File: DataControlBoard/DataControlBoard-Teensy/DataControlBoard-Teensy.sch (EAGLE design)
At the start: 23 parts, among them IC1 74LS165D, IC2 74LS165D, J1 RS-Interface, J2 Pwr-Conn, J3 Static RPi, J4 Magnet RPi, J5 Laser RPi, U1 MAX3232, U2 3V3REG

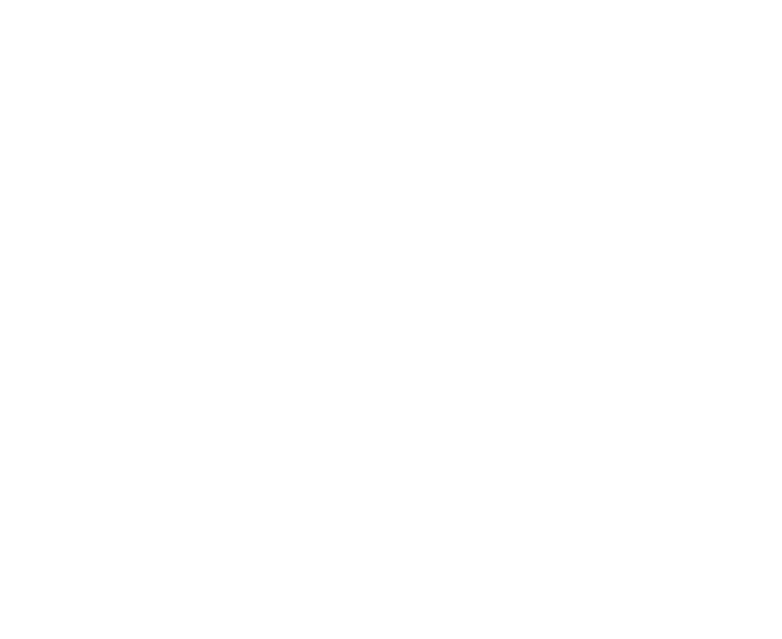
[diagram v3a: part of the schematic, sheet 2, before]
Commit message: Rearranged DataControl-Teensy
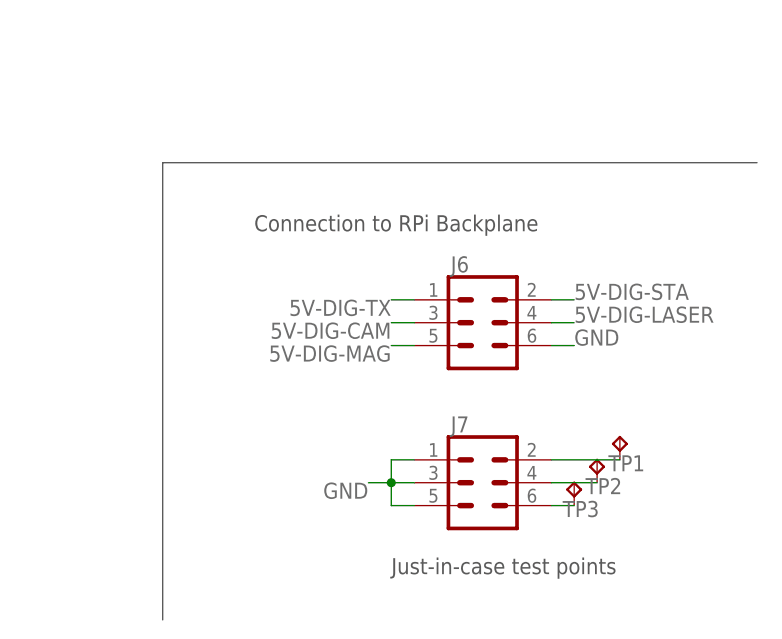
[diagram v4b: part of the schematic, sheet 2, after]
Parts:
- added J6, J7: (no value), SparkFun-Connectors:CONN_03X22X3_SILK_MALE_PTH
- added TP1, TP2, TP3: TPPAD1-17, testpad:TPPAD1-17
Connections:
- new net N$27: J7.4, TP2.TP
- new net N$28: J7.6, TP3.TP
- new net N$6: J7.2, TP1.TP
- net 5V-DIG-CAM: now also J6.3
- net 5V-DIG-LASER: now also J6.4
- net 5V-DIG-MAG: now also J6.5
- net 5V-DIG-STA: now also J6.2
- net 5V-DIG-TX: now also J6.1
- net GND: now also J6.6, J7.1, J7.3, J7.5
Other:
- note added: "Connection to RPi Backplane"
- note added: "Just-in-case test points"
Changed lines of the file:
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@@
 <part name="R8" library="rcl" library_urn="urn:adsk.eagle:library:334" deviceset="R-US_" device="R0805" package3d_urn="urn:adsk.eagle:package:23553/2" value="15k"/>
 <part name="GND5" library="supply1" library_urn="urn:adsk.eagle:library:371" deviceset="GND" device=""/>
+<part name="J6" library="SparkFun-Connectors" library_urn="urn:adsk.eagle:library:513" deviceset="CONN_03X2" device="2X3_SILK_MALE_PTH" package3d_urn="urn:adsk.eagle:package:38016/1"/>
+<part name="J7" library="SparkFun-Connectors" library_urn="urn:adsk.eagle:library:513" deviceset="CONN_03X2" device="2X3_SILK_MALE_PTH" package3d_urn="urn:adsk.eagle:package:38016/1"/>
+<part name="TP1" library="testpad" library_urn="urn:adsk.eagle:library:385" deviceset="TP" device="PAD1-17" package3d_urn="urn:adsk.eagle:package:27949/1"/>
+<part name="TP2" library="testpad" library_urn="urn:adsk.eagle:library:385" deviceset="TP" device="PAD1-17" package3d_urn="urn:adsk.eagle:package:27949/1"/>
+<part name="TP3" library="testpad" library_urn="urn:adsk.eagle:library:385" deviceset="TP" device="PAD1-17" package3d_urn="urn:adsk.eagle:package:27949/1"/>
 </parts>
 <sheets>
@@
 <wire x1="236.22" y1="121.92" x2="236.22" y2="104.14" width="0.1524" layer="97"/>
 <text x="226.06" y="127" size="1.778" layer="97" align="top-left">GPIO from Pi:</text>
+<text x="215.9" y="30.48" size="1.778" layer="97">Just-in-case test points</text>
+<text x="200.66" y="68.58" size="1.778" layer="97">Connection to RPi Backplane</text>
+<wire x1="190.5" y1="25.4" x2="190.5" y2="76.2" width="0.1524" layer="97"/>
+<wire x1="190.5" y1="76.2" x2="256.54" y2="76.2" width="0.1524" layer="97"/>
 </plain>
 <instances>
@@
 <attribute name="NAME" x="35.56" y="98.679" size="1.778" layer="95" font="vector" rot="R180"/>
 <attribute name="VALUE" x="35.56" y="99.441" size="1.778" layer="96" font="vector" rot="R180" align="top-left"/>
+</instance>
+<instance part="J6" gate="G$1" x="226.06" y="58.42" smashed="yes">
+<attribute name="NAME" x="222.504" y="64.008" size="1.778" layer="95" font="vector"/>
+<attribute name="VALUE" x="222.758" y="52.578" size="1.778" layer="96" font="vector" align="top-left"/>
+</instance>
+<instance part="J7" gate="G$1" x="226.06" y="40.64" smashed="yes">
+<attribute name="NAME" x="222.504" y="46.228" size="1.778" layer="95" font="vector"/>
+<attribute name="VALUE" x="222.758" y="34.798" size="1.778" layer="96" font="vector" align="top-left"/>
+</instance>
+<instance part="TP1" gate="G$1" x="241.3" y="45.72" smashed="yes">
+<attribute name="NAME" x="240.03" y="41.91" size="1.778" layer="95"/>
+<attribute name="TP_SIGNAL_NAME" x="242.57" y="44.45" size="1.778" layer="97"/>
+</instance>
+<instance part="TP2" gate="G$1" x="238.76" y="43.18" smashed="yes">
+<attribute name="NAME" x="237.49" y="39.37" size="1.778" layer="95"/>
+<attribute name="TP_SIGNAL_NAME" x="240.03" y="41.91" size="1.778" layer="97"/>
+</instance>
+<instance part="TP3" gate="G$1" x="236.22" y="40.64" smashed="yes">
+<attribute name="NAME" x="234.95" y="36.83" size="1.778" layer="95"/>
+<attribute name="TP_SIGNAL_NAME" x="237.49" y="39.37" size="1.778" layer="97"/>
 </instance>
 </instances>
@@
 </segment>
 </net>
+<net name="GND" class="0">
+<segment>
+<pinref part="J7" gate="G$1" pin="1"/>
+<wire x1="218.44" y1="43.18" x2="215.9" y2="43.18" width="0.1524" layer="91"/>
+<wire x1="215.9" y1="43.18" x2="215.9" y2="40.64" width="0.1524" layer="91"/>
+<pinref part="J7" gate="G$1" pin="5"/>
+<wire x1="215.9" y1="40.64" x2="215.9" y2="38.1" width="0.1524" layer="91"/>
+<wire x1="215.9" y1="38.1" x2="218.44" y2="38.1" width="0.1524" layer="91"/>
+<pinref part="J7" gate="G$1" pin="3"/>
+<wire x1="218.44" y1="40.64" x2="215.9" y2="40.64" width="0.1524" layer="91"/>
+<junction x="215.9" y="40.64"/>
+<wire x1="215.9" y1="40.64" x2="213.36" y2="40.64" width="0.1524" layer="91"/>
+<label x="213.36" y="40.64" size="1.778" layer="95" rot="R180"/>
+</segment>
+<segment>
+<pinref part="J6" gate="G$1" pin="6"/>
+<wire x1="233.68" y1="55.88" x2="236.22" y2="55.88" width="0.1524" layer="91"/>
+<label x="236.22" y="55.88" size="1.778" layer="95"/>
+</segment>
+</net>
+<net name="5V-DIG-LASER" class="0">
+<segment>
+<pinref part="J6" gate="G$1" pin="4"/>
+<wire x1="233.68" y1="58.42" x2="236.22" y2="58.42" width="0.1524" layer="91"/>
+<label x="236.22" y="58.42" size="1.778" layer="95"/>
+</segment>
+</net>
+<net name="5V-DIG-STA" class="0">
+<segment>
+<pinref part="J6" gate="G$1" pin="2"/>
+<wire x1="233.68" y1="60.96" x2="236.22" y2="60.96" width="0.1524" layer="91"/>
+<label x="236.22" y="60.96" size="1.778" layer="95"/>
+</segment>
+</net>
+<net name="5V-DIG-TX" class="0">
+<segment>
+<pinref part="J6" gate="G$1" pin="1"/>
+<wire x1="218.44" y1="60.96" x2="215.9" y2="60.96" width="0.1524" layer="91"/>
+<label x="215.9" y="60.96" size="1.778" layer="95" rot="R180"/>
+</segment>
+</net>
+<net name="5V-DIG-CAM" class="0">
+<segment>
+<pinref part="J6" gate="G$1" pin="3"/>
+<wire x1="218.44" y1="58.42" x2="215.9" y2="58.42" width="0.1524" layer="91"/>
+<label x="215.9" y="58.42" size="1.778" layer="95" rot="R180"/>
+</segment>
+</net>
+<net name="5V-DIG-MAG" class="0">
+<segment>
+<pinref part="J6" gate="G$1" pin="5"/>
+<wire x1="218.44" y1="55.88" x2="215.9" y2="55.88" width="0.1524" layer="91"/>
+<label x="215.9" y="55.88" size="1.778" layer="95" rot="R180"/>
+</segment>
+</net>
+<net name="N$6" class="0">
+<segment>
+<pinref part="J7" gate="G$1" pin="2"/>
+<pinref part="TP1" gate="G$1" pin="TP"/>
+<wire x1="233.68" y1="43.18" x2="241.3" y2="43.18" width="0.1524" layer="91"/>
+</segment>
+</net>
+<net name="N$27" class="0">
+<segment>
+<pinref part="TP2" gate="G$1" pin="TP"/>
+<pinref part="J7" gate="G$1" pin="4"/>
+<wire x1="238.76" y1="40.64" x2="233.68" y2="40.64" width="0.1524" layer="91"/>
+</segment>
+</net>
+<net name="N$28" class="0">
+<segment>
+<pinref part="J7" gate="G$1" pin="6"/>
+<pinref part="TP3" gate="G$1" pin="TP"/>
+<wire x1="233.68" y1="38.1" x2="236.22" y2="38.1" width="0.1524" layer="91"/>
+</segment>
+</net>

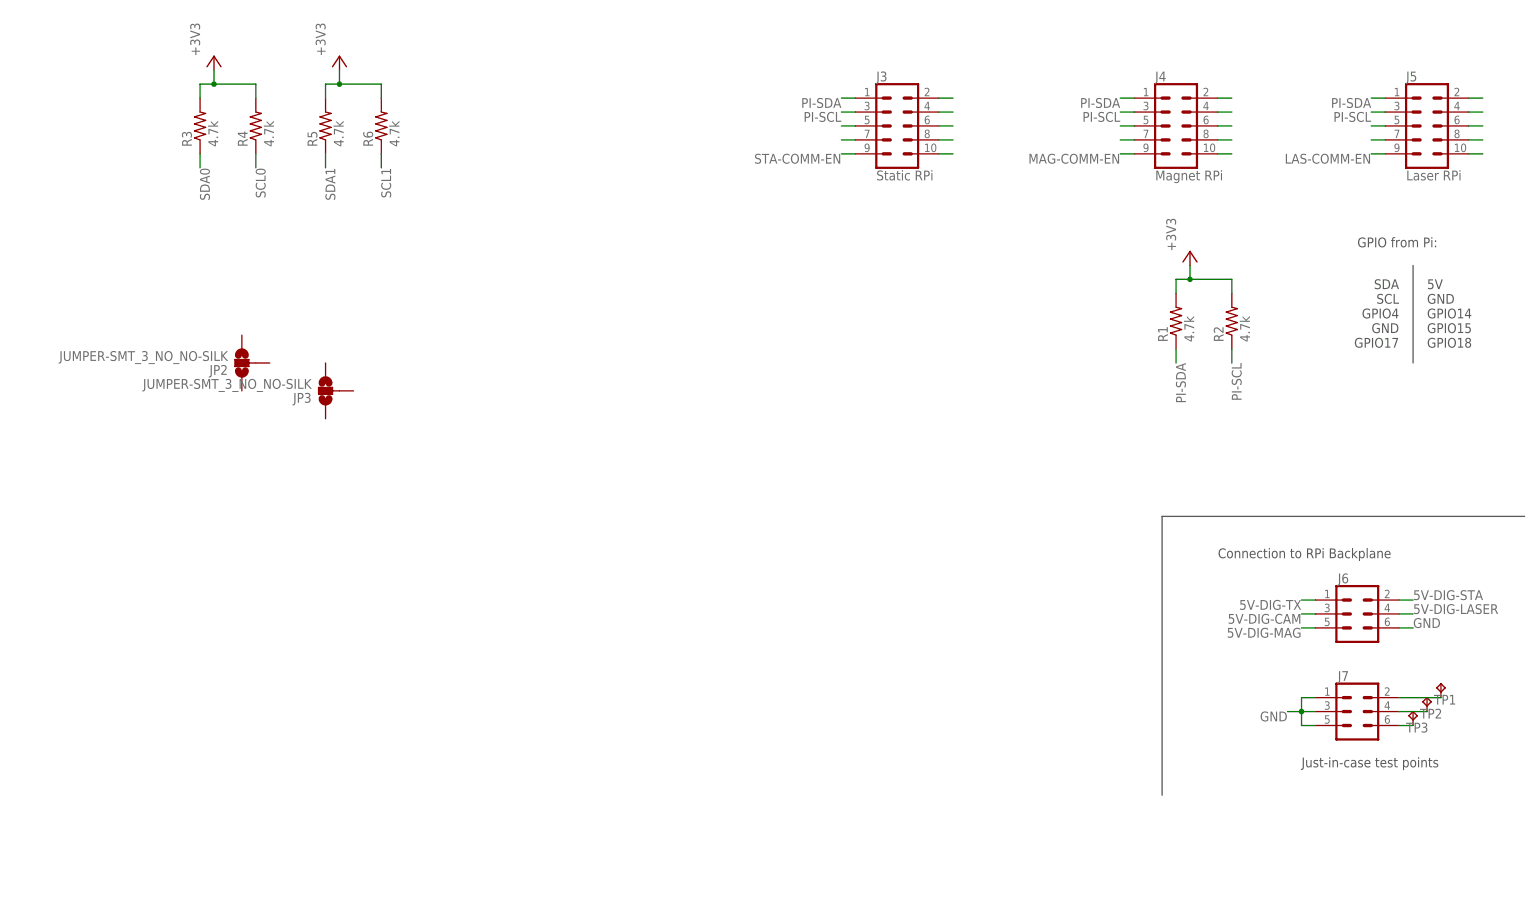
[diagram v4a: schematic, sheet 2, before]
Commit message: Added jumper selection for sda/scl and wired rs232 converter
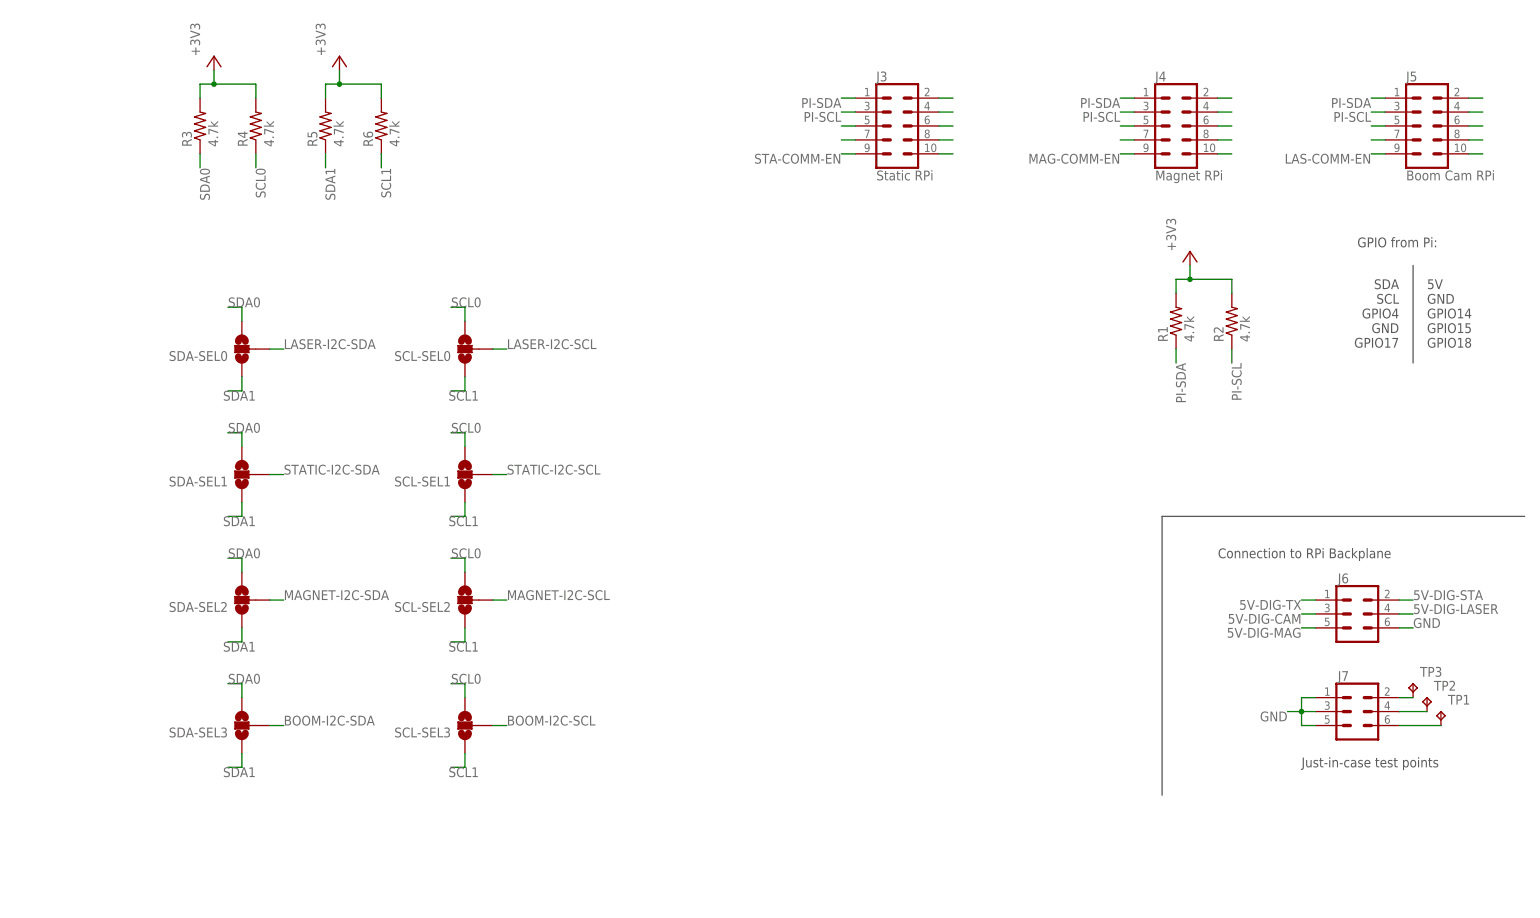
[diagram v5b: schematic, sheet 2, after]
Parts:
- removed JP2, JP3: JUMPER-SMT_3_NO_NO-SILK, SparkFun-Jumpers:JUMPER-SMT_3_NO_NO-SILK
- added C3, C4, C5, C6: 0.1uF, rcl:C-USC0805
- added SCL-SEL0, SCL-SEL1, SCL-SEL2, SCL-SEL3, SDA-SEL0, SDA-SEL1, SDA-SEL2, SDA-SEL3: JUMPER-SMT_3_NO_NO-SILK, SparkFun-Jumpers:JUMPER-SMT_3_NO_NO-SILK
- J5: value Laser RPi -> Boom Cam RPi
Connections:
- removed net N$1: IC1A.CLK, IC2A.CLK
- removed net N$12: B1.3*
- removed net N$20: B1.4*
- removed net N$26: B1.5*
- new net N$32: C5.1, U1.V+
- new net N$33: C6.1, U1.V-
- new net N$34: C3.1, U1.C1+
- new net N$35: C3.2, U1.C1-
- new net N$36: C4.1, U1.C2+
- new net N$37: C4.2, U1.C2-
- new net SHIFT-CLK: B1.4*, IC1A.CLK, IC2A.CLK
- net +3V3: now also U1.VCC
- net BOOM-I2C-SCL: now also SCL-SEL3.2
- net BOOM-I2C-SDA: now also SDA-SEL3.2
- net GND: now also C5.2, C6.2, U1.GND
- net LASER-I2C-SCL: now also SCL-SEL0.2
- net LASER-I2C-SDA: now also SDA-SEL0.2
- net MAGNET-I2C-SCL: now also SCL-SEL2.2
- net MAGNET-I2C-SDA: now also SDA-SEL2.2
- net N$28: now also TP1.TP; no longer TP3.TP
- net N$6: now also TP3.TP; no longer TP1.TP
- net RS232-DATA: now also U1.T1OUT
- net SCL0: now also SCL-SEL0.3, SCL-SEL1.3, SCL-SEL2.3, SCL-SEL3.3
- net SCL1: now also SCL-SEL0.1, SCL-SEL1.1, SCL-SEL2.1, SCL-SEL3.1
- net SDA0: now also SDA-SEL0.3, SDA-SEL1.3, SDA-SEL2.3, SDA-SEL3.3
- net SDA1: now also SDA-SEL0.1, SDA-SEL1.1, SDA-SEL2.1, SDA-SEL3.1
- net SHIFT-IN: now also B1.3*
- net SHIFT-LAT: now also B1.5*
- net STATIC-I2C-SCL: now also SCL-SEL1.2
- net STATIC-I2C-SDA: now also SDA-SEL1.2
- net UART-TX: now also U1.T1IN
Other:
- note added: "Note- Must add inverter and selection for inverter on RS232 line"
- moved on the sheet: TP1, TP3
